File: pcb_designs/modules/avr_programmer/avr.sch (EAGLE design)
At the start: 21 parts, among them IC1 QT9701BD, Q1 12 MHZ, X1 PN61729-S, X2 avr conn

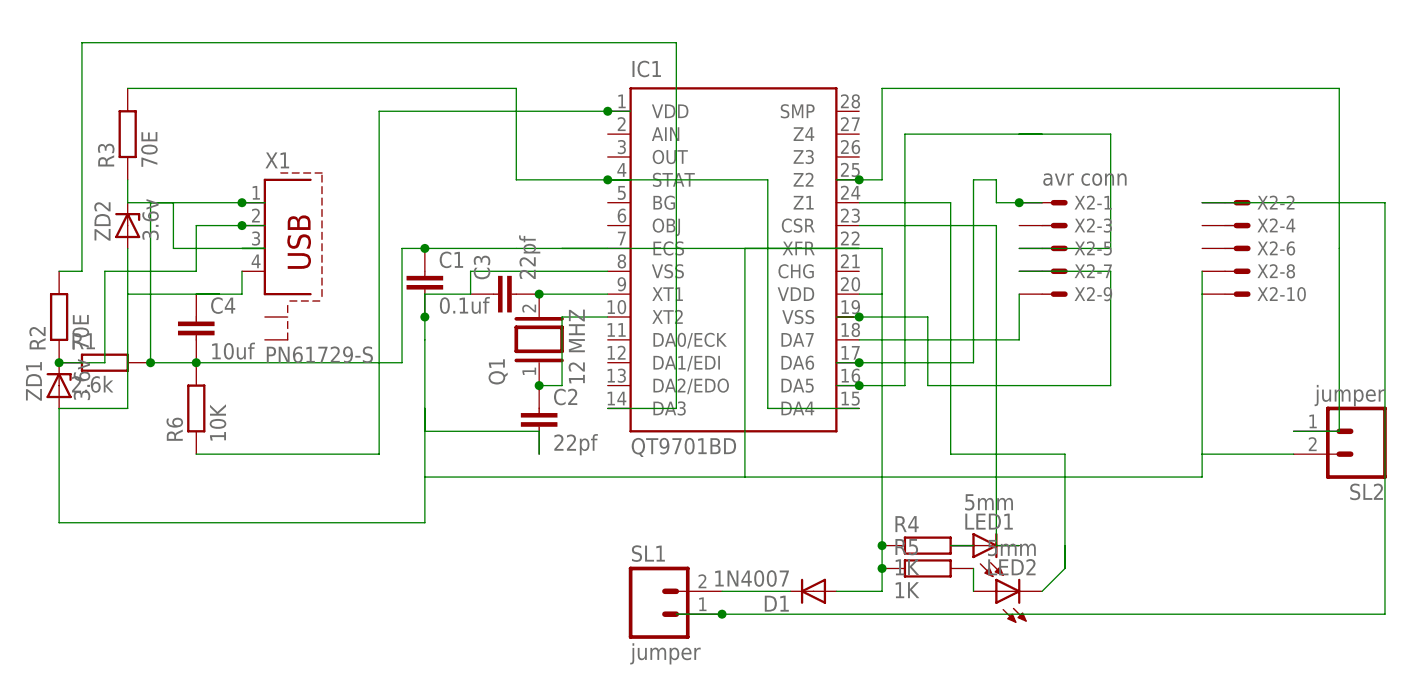
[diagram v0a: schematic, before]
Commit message: 
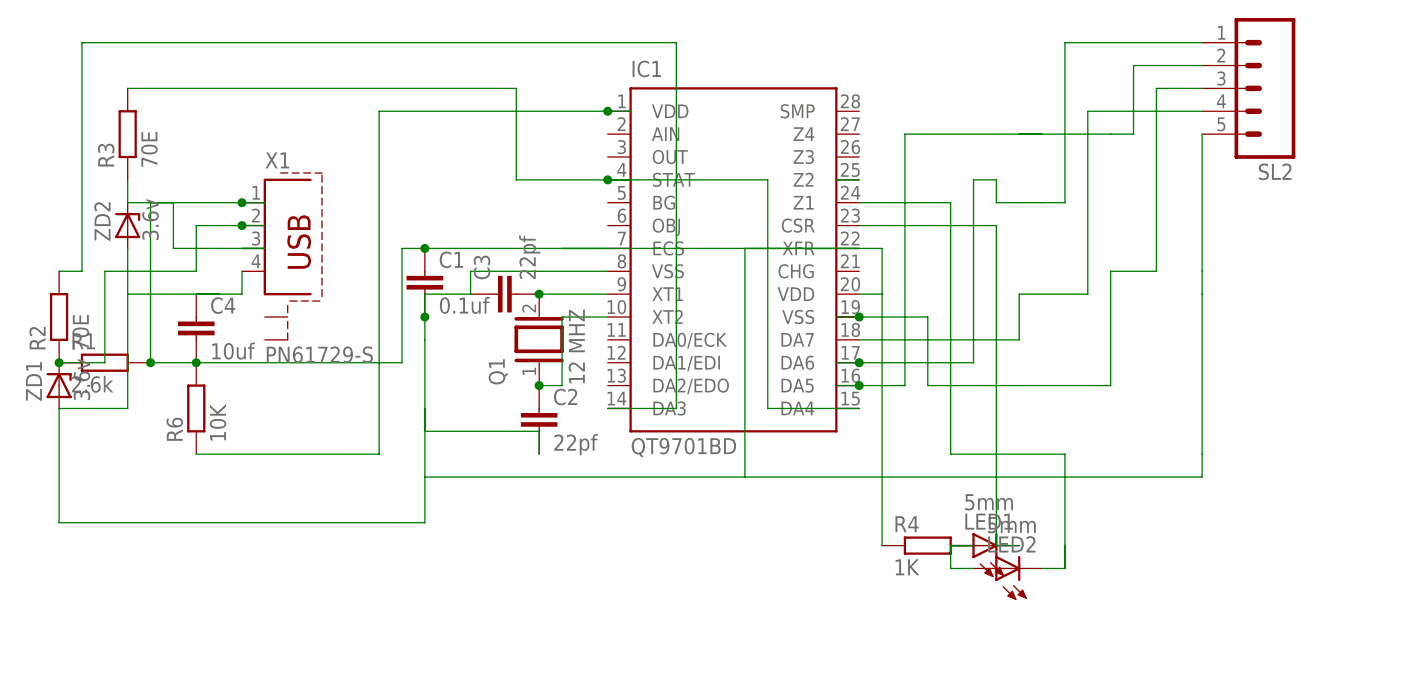
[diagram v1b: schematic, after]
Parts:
- removed D1: 1N4007, diode:1N4004
- removed R5: 1K, resistor:R-EU_0204/7
- removed SL1: jumper, con-amp-quick:M02
- removed X2: avr conn, con-panduit:057-010-1
- LED1, LED2: device led:LED5MM -> led:LED3MM
- SL2: value jumper -> (none); device con-amp-quick:M02 -> con-amp-quick:M05
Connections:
- removed net N$11: D1.C, SL1.2
- removed net N$14: LED2.A, R5.2
- removed net N$15: SL1.1, X2-2.S
- net N$16: now also SL2.1; no longer X2-1.S
- net N$17: now also SL2.2; no longer X2-5.S
- net N$18: now also SL2.3; no longer X2-7.S
- net N$19: now also SL2.4; no longer X2-9.S
- net N$20: no longer SL2.1
- net N$21: now also LED2.A
- net N$5: now also SL2.5; no longer SL2.2, X2-10.S, X2-8.S
- net N$9: no longer D1.A, R5.1
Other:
- moved on the sheet: LED2
